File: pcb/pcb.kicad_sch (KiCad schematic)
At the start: 128 parts, among them J1 Conn_01x05_Female, J2 USB_C_Receptacle_USB2.0, J3 Conn_01x04_Female, SW1 SW_Push, SW2 SW_Push, U1 RP2040, U2 XC6210B332MR-G, U3 GD25Q80CEIGR, Y1 Crystal_GND24

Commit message: added basic layout
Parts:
- J2: footprint 0xLib_USB_Type-C:USB_C_Receptacle_HRO_TYPE-C-31-M-13B -> Connector_USB:USB_C_Receptacle_HRO_TYPE-C-31-M-12
- U1: footprint 0xLib_Package_DFN_QFN:QFN-56-1EP_7x7mm_P0.4mm_EP3.2x3.2mm -> Package_DFN_QFN:QFN-56-1EP_7x7mm_P0.4mm_EP3.2x3.2mm
- U3: footprint 0xLib_Package_DFN_QFN:USON-8-1EP_3x2mm_P0.5mm_EP0.25x1.65mm -> Package_SON:Texas_R-PUSON-N8_USON-8-1EP_1.6x2.1mm_P0.5mm_EP0.4x1.7mm
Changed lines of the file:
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@@
 			)
 		)
-		(property "Footprint" "0xLib_Package_DFN_QFN:QFN-56-1EP_7x7mm_P0.4mm_EP3.2x3.2mm"
+		(property "Footprint" "Package_DFN_QFN:QFN-56-1EP_7x7mm_P0.4mm_EP3.2x3.2mm"
 			(at 156.21 100.33 0)
 			(effects
@@
 			)
 		)
-		(property "Footprint" "0xLib_USB_Type-C:USB_C_Receptacle_HRO_TYPE-C-31-M-13B"
+		(property "Footprint" "Connector_USB:USB_C_Receptacle_HRO_TYPE-C-31-M-12"
 			(at 41.91 57.15 0)
 			(effects
@@
 			)
 		)
-		(property "Footprint" "0xLib_Package_DFN_QFN:USON-8-1EP_3x2mm_P0.5mm_EP0.25x1.65mm"
+		(property "Footprint" "Package_SON:Texas_R-PUSON-N8_USON-8-1EP_1.6x2.1mm_P0.5mm_EP0.4x1.7mm"
 			(at 246.38 137.16 0)
 			(effects

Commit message: fixed connections
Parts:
- added J4, J5, J6, J7: Conn_01x05, Connector_JST:JST_GH_SM05B-GHS-TB_1x05-1MP_P1.25mm_Horizontal, symbol Connector_Generic:Conn_01x05
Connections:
- net col0 is gone; now on net COL0: D1.1 (K), D13.1 (K), D7.1 (K)
- net col1 is gone; now on net COL1: D14.1 (K), D2.1 (K), D8.1 (K)
- net col2 is gone; now on net COL2: D15.1 (K), D19.1 (K), D3.1 (K), D9.1 (K)
- net col3 is gone; now on net COL3: D10.1 (K), D16.1 (K), D20.1 (K), D4.1 (K)
- net col4 is gone; now on net COL4: D11.1 (K), D17.1 (K), D21.1 (K), D5.1 (K)
- net col5 is gone; now on net COL5: D12.1 (K), D18.1 (K), D22.1 (K), D6.1 (K)
- net COL6: now also J4.5 (Pin_5)
- net COL7: now also J6.1 (Pin_1)
- net COL8: now also J6.2 (Pin_2)
- net COL9: now also J6.3 (Pin_3)
- net ROW0: now also MX1.1, MX2.1, MX3.1, MX4.1, MX5.1, MX6.1, J4.1 (Pin_1), J5.1 (Pin_1)
- net ROW1: now also MX10.1, MX11.1, MX12.1, MX7.1, MX8.1, MX9.1, J4.2 (Pin_2), J5.2 (Pin_2)
- net ROW2: now also MX13.1, MX14.1, MX15.1, MX16.1, MX17.1, MX18.1, J4.3 (Pin_3), J5.3 (Pin_3)
- net ROW3: now also MX19.1, MX20.1, MX21.1, MX22.1, MX45.1, J4.4 (Pin_4), J5.4 (Pin_4)
- net COL10: now reaches U1.13 (GPIO10)
- net COL10: now also J6.4 (Pin_4)
- net COL11: now reaches U1.14 (GPIO11)
- net COL11: now also J6.5 (Pin_5)
- net col10 renamed COL10r
- net COL10r: now also J7.4 (Pin_4)
- net col11 renamed COL11r
- net COL11r: now also J7.5 (Pin_5)
- net col6 renamed COL6r
- net COL6r: now also J5.5 (Pin_5)
- net col7 renamed COL7r
- net COL7r: now also J7.1 (Pin_1)
- net col8 renamed COL8r
- net COL8r: now also J7.2 (Pin_2)
- net col9 renamed COL9r
- net COL9r: now also J7.3 (Pin_3)
- net row0 renamed ROW0r
- net ROW0r: no longer MX1.1, MX2.1, MX3.1, MX4.1, MX5.1, MX6.1
- net row1 renamed ROW1r
- net ROW1r: no longer MX10.1, MX11.1, MX12.1, MX7.1, MX8.1, MX9.1
- net row2 renamed ROW2r
- net ROW2r: no longer MX13.1, MX14.1, MX15.1, MX16.1, MX17.1, MX18.1
- net row3 renamed ROW3r
- net ROW3r: no longer MX19.1, MX20.1, MX21.1, MX22.1, MX45.1
- no-connect marks 10 -> 8

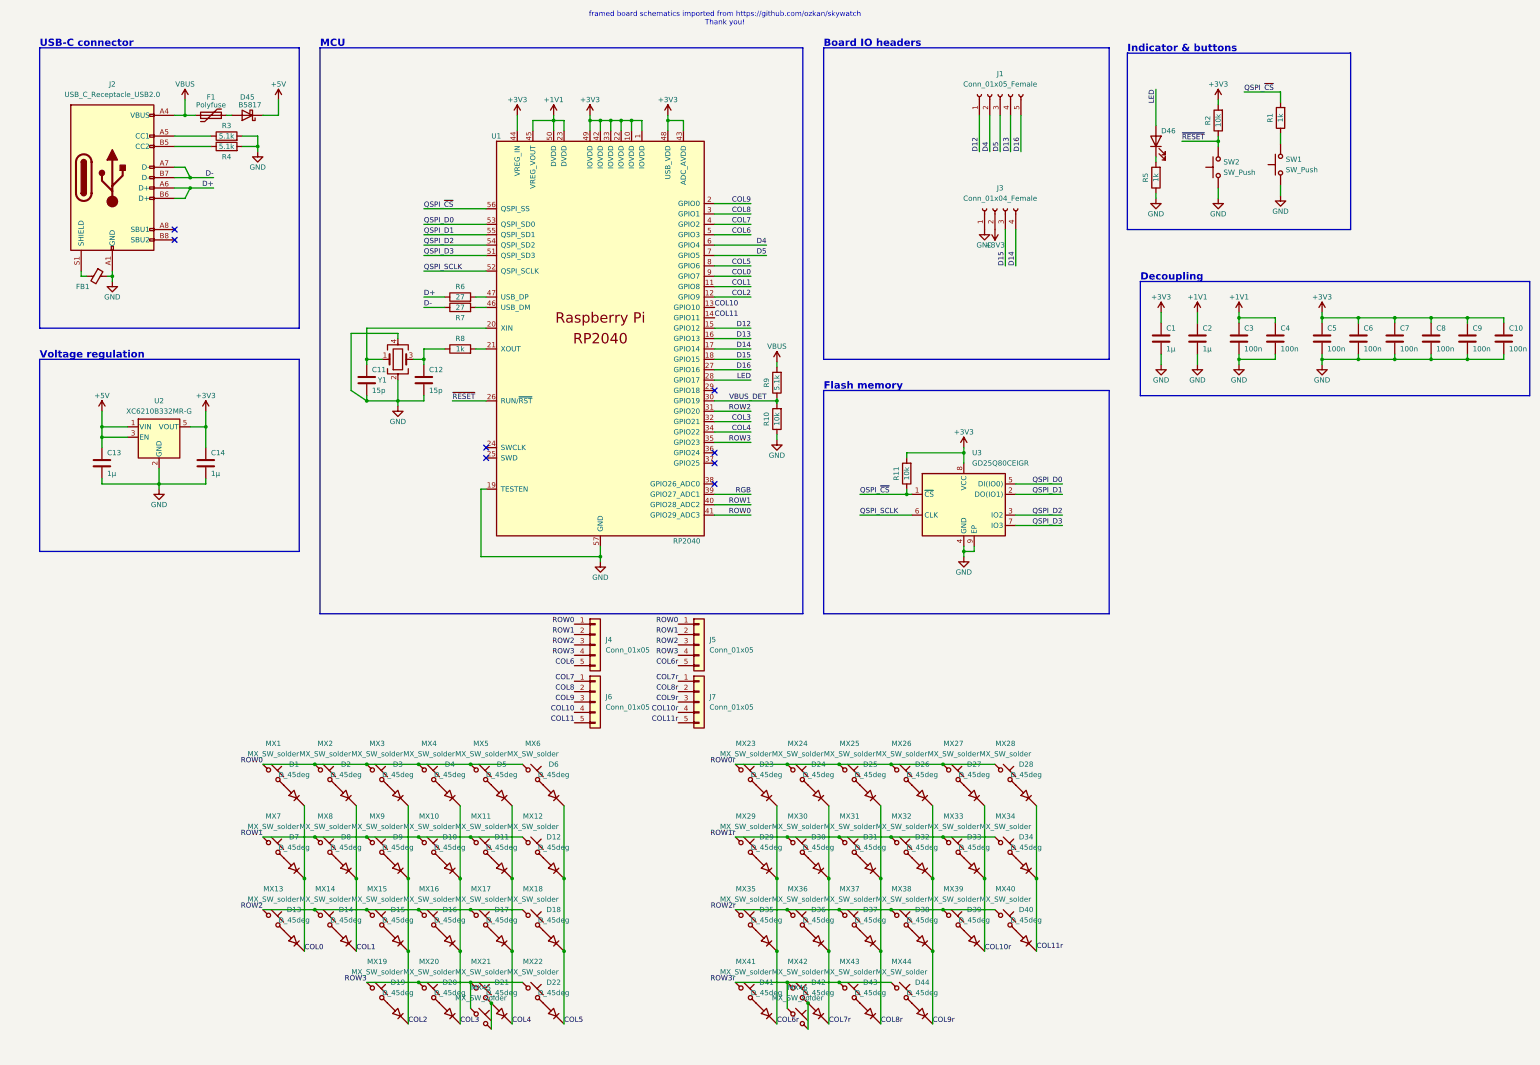
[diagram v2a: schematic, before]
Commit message: imported template for rp2040 components
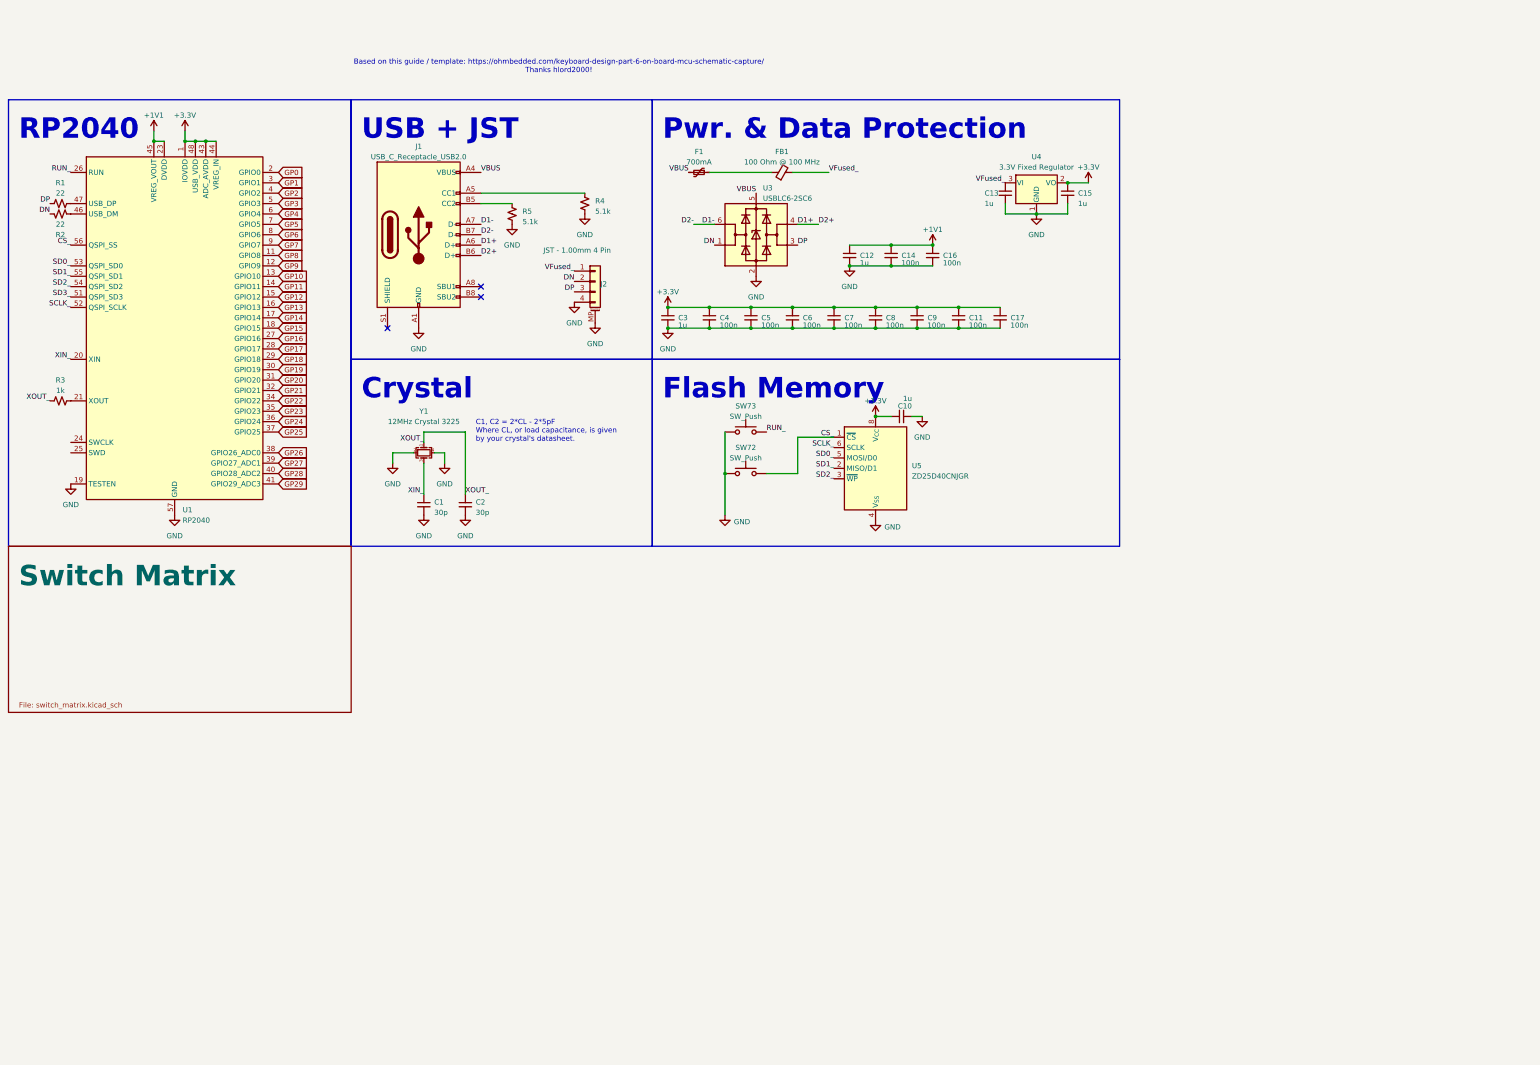
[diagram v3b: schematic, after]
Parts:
- removed C1, C2: 1µ, Capacitor_SMD:C_0402_1005Metric, symbol Device:C
- removed C10, C3, C4, C5, C6, C7, C8, C9: 100n, Capacitor_SMD:C_0402_1005Metric, symbol Device:C
- removed C11, C12: 15p, Capacitor_SMD:C_0402_1005Metric, symbol Device:C
- removed C13, C14: 1µ, Capacitor_SMD:C_0603_1608Metric, symbol Device:C
- removed D1, D10, D11, D12, D13, D14, D15, D16, D17, D18, D19, D2, D20, D21, D22, D23, D24, D25, D26, D27, D28, D29, D3, D30, D31, D32, D33, D34, D35, D36, D37, D38, D39, D4, D40, D41, D42, D43, D44, D5, D6, D7, D8, D9: D_45deg, pcb:D_SOD-123-minimal, symbol Device:D_45deg
- removed D45: B5817, Diode_SMD:D_SOD-323, symbol Device:D_Schottky
- removed D46: LED, LED_SMD:LED_0402_1005Metric, symbol Device:LED
- removed F1: Polyfuse, Fuse:Fuse_0603_1608Metric, symbol Device:Polyfuse
- removed J1: Conn_01x05_Female, Connector_PinHeader_2.54mm:PinHeader_1x05_P2.54mm_Vertical, symbol Connector:Conn_01x05_Female
- removed J2: USB_C_Receptacle_USB2.0, Connector_USB:USB_C_Receptacle_HRO_TYPE-C-31-M-12, symbol Connector:USB_C_Receptacle_USB2.0
- removed J3: Conn_01x04_Female, Connector_PinHeader_2.54mm:PinHeader_1x04_P2.54mm_Vertical, symbol Connector:Conn_01x04_Female
- removed J4, J5, J6, J7: Conn_01x05, Connector_JST:JST_GH_SM05B-GHS-TB_1x05-1MP_P1.25mm_Horizontal, symbol Connector_Generic:Conn_01x05
- removed MX1, MX10, MX11, MX12, MX13, MX14, MX15, MX16, MX17, MX18, MX19, MX2, MX20, MX21, MX22, MX23, MX24, MX25, MX26, MX27, MX28, MX29, MX3, MX30, MX31, MX32, MX33, MX34, MX35, MX36, MX37, MX38, MX39, MX4, MX40, MX41, MX42, MX43, MX44, MX45, MX46, MX5, MX6, MX7, MX8, MX9: MX_SW_solder, PCM_marbastlib-mx:SW_MX_1u, symbol PCM_marbastlib-mx:MX_SW_solder
- removed R1, R5, R8: 1k, Resistor_SMD:R_0402_1005Metric, symbol Device:R
- removed R10, R11, R2: 10k, Resistor_SMD:R_0402_1005Metric, symbol Device:R
- removed R3, R4, R9: 5.1k, Resistor_SMD:R_0402_1005Metric, symbol Device:R
- removed R6, R7: 27, Resistor_SMD:R_0402_1005Metric, symbol Device:R
- removed SW1, SW2: SW_Push, Button_Switch_SMD:SW_SPST_CK_KXT3, symbol Switch:SW_Push
- removed U1: RP2040, Package_DFN_QFN:QFN-56-1EP_7x7mm_P0.4mm_EP3.2x3.2mm, symbol MCU_RaspberryPi_RP2040:RP2040
- removed U2: XC6210B332MR-G, Package_TO_SOT_SMD:SOT-23-5, symbol Regulator_Linear:AP2127K-3.3
- removed U3: GD25Q80CEIGR, Package_SON:Texas_R-PUSON-N8_USON-8-1EP_1.6x2.1mm_P0.5mm_EP0.4x1.7mm, symbol Memory_Flash:W25Q32JVZP
- removed Y1: Crystal_GND24, Crystal:Crystal_SMD_2520-4Pin_2.5x2.0mm, symbol Device:Crystal_GND24
- added C1, C2: 30p, Capacitor_SMD:C_0402_1005Metric, symbol Device:C_Small
- added C10, C12, C13, C15, C3: 1u, Capacitor_SMD:C_0402_1005Metric, symbol Device:C_Small
- added C11, C14, C16, C17, C4, C5, C6, C7, C8, C9: 100n, Capacitor_SMD:C_0402_1005Metric, symbol Device:C_Small
- added F1: 700mA, Fuse:Fuse_0402_1005Metric, symbol Device:Polyfuse_Small
- added J1: USB_C_Receptacle_USB2.0, Connector_USB:USB_C_Receptacle_GCT_USB4110, symbol Connector:USB_C_Receptacle_USB2.0
- added J2: JST - 1.00mm 4 Pin, Connector_JST:JST_SH_SM04B-SRSS-TB_1x04-1MP_P1.00mm_Horizontal, symbol Connector_Generic_MountingPin:Conn_01x04_MountingPin
- added R1, R2: 22, Resistor_SMD:R_0402_1005Metric, symbol Device:R_Small_US
- added R3: 1k, Resistor_SMD:R_0402_1005Metric, symbol Device:R_Small_US
- added R4, R5: 5.1k, Resistor_SMD:R_0402_1005Metric, symbol Device:R_Small_US
- added SW72, SW73: SW_Push, Button_Switch_SMD:SW_SPST_SKQG_WithoutStem, symbol Switch:SW_Push
- added U1: RP2040, Package_DFN_QFN:QFN-56-1EP_7x7mm_P0.4mm_EP3.2x3.2mm_ThermalVias, symbol MCU_RaspberryPi:RP2040
- added U3: USBLC6-2SC6, Package_TO_SOT_SMD:SOT-23-6, symbol Power_Protection:USBLC6-2SC6
- added U4: 3.3V Fixed Regulator, Package_TO_SOT_SMD:TSOT-23, symbol Regulator_Linear:AP2127N3-1.2
- added U5: ZD25D40CNJGR, USON8:USON-8_1.5x1.5mm_P0.45mm, symbol Flash_NOR_SPI:ZD25D40CNJGR
- added Y1: 12MHz Crystal 3225, Crystal:Crystal_SMD_3225-4Pin_3.2x2.5mm, symbol Device:Crystal_GND24_Small
- FB1: value FerriteBead_Small -> 100 Ohm @ 100 MHz; footprint Inductor_SMD:L_0603_1608Metric -> Inductor_SMD:L_0402_1005Metric; LCSC C98288 -> C85812
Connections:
- net +1V1: now also C12.1, C14.1, C16.1, U1.23 (DVDD), U1.45 (VREG_VOUT), U1.50 (DVDD)
- net GND: now also C1.2, C10.2, C11.2, C12.2, C13.2, C14.2, C15.2, C16.2, C17.2, C2.2, C3.2, C4.2, C5.2, C6.2, C7.2, C8.2, C9.2, J1.A1 (GND), J1.A12 (GND), J1.B1 (GND), J1.B12 (GND), J2.4 (Pin_4), J2.MP (MountPin), R4.1, R5.1, SW72.1, SW73.1, U1.19 (TESTEN), U1.57 (GND), U3.2 (GND), U4.1 (GND), U5.4 (V_{SS}), U5.9 (PAD/V_{SS}), Y1.2, Y1.4; no longer FB1.1
- net VBUS: now also F1.2, J1.A4 (VBUS), J1.A9 (VBUS), J1.B4 (VBUS), J1.B9 (VBUS), U3.5 (VBUS)
- net VFused_: now reaches FB1.2
- net VFused_: now also C13.1, J2.1 (Pin_1), U4.3 (VI)
- new net: F1.1, FB1.1
- new net: R3.2, U1.21 (XOUT)
- new net: R1.2, U1.47 (USB_DP)
- new net: J1.A5 (CC1), R4.2
- new net: J1.B5 (CC2), R5.2
- new net: R2.1, U1.46 (USB_DM)
- new net +3.3V: C10.1, C11.1, C15.1, C17.1, C3.1, C4.1, C5.1, C6.1, C7.1, C8.1, C9.1, U1.1 (IOVDD), U1.10 (IOVDD), U1.22 (IOVDD), U1.33 (IOVDD), U1.42 (IOVDD), U1.43 (ADC_AVDD), U1.44 (VREG_IN), U1.48 (USB_VDD), U1.49 (IOVDD), U4.2 (VO), U5.8 (V_{CC})
- new net CS_: SW72.2, U1.56 (QSPI_SS), U5.1 (~{CS})
- new net D1+: J1.A6 (D+), J1.B6 (D+), U3.4 (I/O2)
- new net D1-: J1.A7 (D-), J1.B7 (D-), U3.6 (I/O1)
- new net DN: J2.2 (Pin_2), R2.2, U3.1 (I/O1)
- new net DP: J2.3 (Pin_3), R1.1, U3.3 (I/O2)
- new net GP0: U1.2 (GPIO0)
- new net GP1: U1.3 (GPIO1)
- new net GP10: U1.13 (GPIO10)
- new net GP11: U1.14 (GPIO11)
- new net GP12: U1.15 (GPIO12)
- new net GP13: U1.16 (GPIO13)
- new net GP14: U1.17 (GPIO14)
- new net GP15: U1.18 (GPIO15)
- new net GP16: U1.27 (GPIO16)
- new net GP17: U1.28 (GPIO17)
- new net GP18: U1.29 (GPIO18)
- new net GP19: U1.30 (GPIO19)
- new net GP2: U1.4 (GPIO2)
- new net GP20: U1.31 (GPIO20)
- new net GP21: U1.32 (GPIO21)
- new net GP22: U1.34 (GPIO22)
- new net GP23: U1.35 (GPIO23)
- new net GP24: U1.36 (GPIO24)
- new net GP25: U1.37 (GPIO25)
- new net GP26: U1.38 (GPIO26_ADC0)
- new net GP27: U1.39 (GPIO27_ADC1)
- new net GP28: U1.40 (GPIO28_ADC2)
- new net GP29: U1.41 (GPIO29_ADC3)
- new net GP3: U1.5 (GPIO3)
- new net GP4: U1.6 (GPIO4)
- new net GP5: U1.7 (GPIO5)
- new net GP6: U1.8 (GPIO6)
- new net GP7: U1.9 (GPIO7)
- new net GP8: U1.11 (GPIO8)
- new net GP9: U1.12 (GPIO9)
- new net RUN_: SW73.2, U1.26 (RUN)
- new net SCLK_: U1.52 (QSPI_SCLK), U5.6 (SCLK)
- new net SD0_: U1.53 (QSPI_SD0), U5.5 (MOSI/D0)
- new net SD1_: U1.55 (QSPI_SD1), U5.2 (MISO/D1)
- new net SD2_: U1.54 (QSPI_SD2), U5.3 (~{WP})
- new net SD3_: U1.51 (QSPI_SD3)
- new net XIN_: C1.1, U1.20 (XIN), Y1.3
- new net XOUT_: C2.1, R3.1, Y1.1
- no-connect marks 8 -> 3
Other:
- added sheet Switch Matrix (switch_matrix.kicad_sch)
- note added: "Based on this guide / template: https://ohmbedded.com/keyboard-design-part-6-on-board-mcu-schematic-capture/ Thanks hlord2000!"
- note added: "C1, C2 = 2*CL - 2*5pF Where CL, or load capacitance, is given by your crystal's datasheet."
- note added: "Crystal"
- note added: "Flash Memory"
- note added: "Pwr. & Data Protection"
- note added: "RP2040"
- note added: "USB + JST"
- note removed: "Board IO headers"
- note removed: "Decoupling"
- note removed: "Flash memory"
- note removed: "Indicator & buttons"
- note removed: "MCU"
- note removed: "USB-C connector"
- note removed: "Voltage regulation"
- note removed: "framed board schematics imported from https://github.com/ozkan/skywatch Thank you!"

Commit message: added some more routing
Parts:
- removed J2: JST - 1.00mm 4 Pin, Connector_JST:JST_SH_SM04B-SRSS-TB_1x04-1MP_P1.00mm_Horizontal, symbol Connector_Generic_MountingPin:Conn_01x04_MountingPin
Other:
- note added: "USB"
- note removed: "USB + JST"
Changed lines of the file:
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@@
 		)
 	)
-	(text "USB + JST"
+	(text "USB"
 		(exclude_from_sim no)
 		(at 99.06 48.26 0)
@@
 		)
 	)
-	(label "DP"
-		(at 151.13 85.09 180)
-		(effects
-			(font
-				(size 1.27 1.27)
-			)
-			(justify right bottom)
-		)
-	)
 	(label "XOUT_"
 		(at 114.3 121.92 180)
@@
 		)
 	)
-	(label "DN"
-		(at 151.13 82.55 180)
-		(effects
-			(font
-				(size 1.27 1.27)
-			)
-			(justify right bottom)
-		)
-	)
 	(label "RUN_"
 		(at 27.94 55.88 180)
@@
 		)
 	)
-	(label "VFused_"
-		(at 151.13 80.01 180)
-		(effects
-			(font
-				(size 1.27 1.27)
-			)
-			(justify right bottom)
-		)
-	)
 	(label "XOUT_"
 		(at 124.46 134.62 0)
@@
 	)
 	(symbol
-		(lib_id "Connector_Generic_MountingPin:Conn_01x04_MountingPin")
-		(at 156.21 82.55 0)
-		(unit 1)
-		(exclude_from_sim no)
-		(in_bom yes)
-		(on_board yes)
-		(dnp no)
-		(property "Reference" "J2"
-			(at 157.48 83.185 0)
-			(effects
-				(font
-					(size 1.27 1.27)
-				)
-				(justify left)
-			)
-		)
-		(property "Value" "JST - 1.00mm 4 Pin"
-			(at 143.51 74.93 0)
-			(effects
-				(font
-					(size 1.27 1.27)
-				)
-				(justify left)
-			)
-		)
-		(property "Footprint" "Connector_JST:JST_SH_SM04B-SRSS-TB_1x04-1MP_P1.00mm_Horizontal"
-			(at 156.21 82.55 0)
-			(effects
-				(font
-					(size 1.27 1.27)
-				)
-				(hide yes)
-			)
-		)
-		(property "Datasheet" "~"
-			(at 156.21 82.55 0)
-			(effects
-				(font
-					(size 1.27 1.27)
-				)
-				(hide yes)
-			)
-		)
-		(property "Description" ""
-			(at 156.21 82.55 0)
-			(effects
-				(font
-					(size 1.27 1.27)
-				)
-			)
-		)
-		(property "LCSC" "C160404"
-			(at 156.21 82.55 0)
-			(effects
-				(font
-					(size 1.27 1.27)
-				)
-				(hide yes)
-			)
-		)
-		(pin "1"
-		)
-		(pin "2"
-		)
-		(pin "3"
-		)
-		(pin "4"
-		)
-		(pin "MP"
-		)
-		(instances
-			(project ""
-				(path "/dea5f69c-d02e-47df-8e1a-a63949fabb21"
-					(reference "J2")
-					(unit 1)
-				)
-			)
-		)
-	)
-	(symbol
 		(lib_id "Device:C_Small")
 		(at 234.95 91.44 0)
@@
 	)
 	(symbol
-		(lib_id "power:GND")
-		(at 151.13 87.63 0)
-		(unit 1)
-		(exclude_from_sim no)
-		(in_bom yes)
-		(on_board yes)
-		(dnp no)
-		(fields_autoplaced yes)
-		(property "Reference" "#PWR012"
-			(at 151.13 93.98 0)
-			(effects
-				(font
-					(size 1.27 1.27)
-				)
-				(hide yes)
-			)
-		)
-		(property "Value" "GND"
-			(at 151.13 92.71 0)
-			(effects
-				(font
-					(size 1.27 1.27)
-				)
-			)
-		)
-		(property "Footprint" ""
-			(at 151.13 87.63 0)
-			(effects
-				(font
-					(size 1.27 1.27)
-				)
-				(hide yes)
-			)
-		)
-		(property "Datasheet" ""
-			(at 151.13 87.63 0)
-			(effects
-				(font
-					(size 1.27 1.27)
-				)
-				(hide yes)
-			)
-		)
-		(property "Description" ""
-			(at 151.13 87.63 0)
-			(effects
-				(font
-					(size 1.27 1.27)
-				)
-			)
-		)
-		(pin "1"
-		)
-		(instances
-			(project ""
-				(path "/dea5f69c-d02e-47df-8e1a-a63949fabb21"
-					(reference "#PWR012")
-					(unit 1)
-				)
-			)
-		)
-	)
-	(symbol
 		(lib_id "MCU_RaspberryPi:RP2040")
 		(at 53.34 93.98 0)
@@
 					(unit 1)
 				)
-			)
-		)
-	)
-	(symbol
-		(lib_id "power:GND")
-		(at 156.21 92.71 0)
-		(unit 1)
-		(exclude_from_sim no)
-		(in_bom yes)
-		(on_board yes)
-		(dnp no)
-		(fields_autoplaced yes)
-		(property "Reference" "#PWR011"
-			(at 156.21 99.06 0)
-			(effects
-				(font
-					(size 1.27 1.27)
-				)
-				(hide yes)
-			)
-		)
-		(property "Value" "GND"
-			(at 156.21 97.79 0)
-			(effects
-				(font
-					(size 1.27 1.27)
-				)
-			)
-		)
-		(property "Footprint" ""
-			(at 156.21 92.71 0)
-			(effects
-				(font
-					(size 1.27 1.27)
-				)
-				(hide yes)
-			)
-		)
-		(property "Datasheet" ""
-			(at 156.21 92.71 0)
-			(effects
-				(font
-					(size 1.27 1.27)
-				)
-				(hide yes)
-			)
-		)
-		(property "Description" ""
-			(at 156.21 92.71 0)
-			(effects
-				(font
-					(size 1.27 1.27)
-				)
-			)
-		)
-		(pin "1"
-		)
-		(instances
-			(project ""
-				(path "/dea5f69c-d02e-47df-8e1a-a63949fabb21"
-					(reference "#PWR011")
-					(unit 1)
-				)

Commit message: redid routing
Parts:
- added H1, H2, H3, H4, H5, H6, H7, H8: MountingHole, pcb:spacer_hole_4mm, symbol Mechanical:MountingHole
